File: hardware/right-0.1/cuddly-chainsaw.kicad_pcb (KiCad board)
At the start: 2 copper layers, 3.7 x 3.7 mm, 107 parts, among them J1 USB_C_Receptacle_USB2.0, J2 USB_C_Receptacle_USB2.0, SW1 Encoder_MX_RGB, SW10 MX_RGB, SW11 MX_RGB, SW12 MX_RGB, SW13 MX_RGB, SW14 MX_RGB, SW15 MX_RGB, SW16 MX_RGB, SW17 MX_RGB, SW18 MX_RGB, SW19 MX_RGB, SW2 MX_RGB, SW20 MX_RGB, SW21 MX_RGB, SW22 MX_RGB, SW23 MX_RGB, SW24 MX_RGB, SW25 MX_RGB, SW26 MX_RGB, SW27 MX_RGB, SW28 MX_RGB, SW29 MX_RGB, SW3 MX_RGB, SW30 MX_RGB, SW31 MX_RGB, SW32 MX_RGB, SW33 MX_RGB, SW34 MX_RGB, SW35 SW_Push, SW36 MX_RGB, SW37 MX_RGB, SW38 MX_RGB, SW39 MX_RGB, SW4 MX_RGB, SW40 MX_RGB, SW41 MX_RGB, SW42 MX_RGB, SW5 MX_RGB, SW6 MX_RGB, SW7 MX_RGB, SW8 MX_RGB, SW9 MX_RGB, U1 USBLC6-2SC6, U2 ATmega32U4-MU, Y1 16MHz

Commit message: first go at board outline done
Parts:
- SW14: footprint josh-buttons-switches:MX_KEYSWITCH_RGB -> josh-buttons-switches:MX_KEYSWITCH_RGB_1.75U
- SW37: footprint josh-buttons-switches:MX_KEYSWITCH_RGB -> josh-buttons-switches:MX_KEYSWITCH_RGB_2.5U
- SW6: footprint josh-buttons-switches:MX_KEYSWITCH_RGB -> josh-buttons-switches:MX_KEYSWITCH_RGB_2U
- SW7: footprint josh-buttons-switches:MX_KEYSWITCH_RGB -> josh-buttons-switches:MX_KEYSWITCH_RGB_1.5U
- SW8: footprint josh-buttons-switches:MX_KEYSWITCH_RGB -> josh-buttons-switches:MX_KEYSWITCH_RGB_2.25U
- U2: moved to B.Cu
- moved SW1 184.5 mm to (221.7, 56.3)
- moved SW2 184.5 mm to (221.7, 75.4)
- moved SW4 184.5 mm to (221.7, 113.5)
- moved SW5 184.5 mm to (221.7, 132.5)
- moved SW3 184.5 mm to (221.7, 94.5)
- moved J2 182.1 mm to (78.5, 49.8)
- moved D3 158.3 mm to (202.7, 113.5)
- moved D6 158.2 mm to (221.7, 56.3)
- moved D5 149.1 mm to (193.3, 56.3)
- moved D4 146.7 mm to (191.5, 129.2)
- moved SW10 146.7 mm to (202.7, 132.5)
- moved SW9 146.7 mm to (202.6, 113.5)
- moved SW7 142.0 mm to (197.9, 75.4)
- moved D1 141.9 mm to (186.8, 72.2)
- moved BZ1 139.5 mm to (112.2, 133.2)
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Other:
- board size 3.7 x 3.7 mm -> 181 x 100.8 mm

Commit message: left all connected
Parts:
- added C10: 100n, Capacitor_SMD:C_0603_1608Metric, B.Cu at (265.0, 94.5)
- added C11: 100n, Capacitor_SMD:C_0603_1608Metric, B.Cu at (270.0, 90.5)
- added C12: 100n, Capacitor_SMD:C_0603_1608Metric, B.Cu at (262.5, 98.5)
- added C13: 100n, Capacitor_SMD:C_0603_1608Metric, B.Cu at (256.8, 103.7)
- added C14: 100n, Capacitor_SMD:C_0603_1608Metric, B.Cu at (267.5, 94.5)
- added C15: 100n, Capacitor_SMD:C_0603_1608Metric, B.Cu at (256.8, 123.8)
- added C16: 100n, Capacitor_SMD:C_0603_1608Metric, B.Cu at (256.8, 115.7)
- added C17: 100n, Capacitor_SMD:C_0603_1608Metric, B.Cu at (260.0, 98.5)
- added C18: 100n, Capacitor_SMD:C_0603_1608Metric, B.Cu at (276.6, 90.1)
- added C19: 100n, Capacitor_SMD:C_0603_1608Metric, B.Cu at (256.8, 111.7)
- added C20: 100n, Capacitor_SMD:C_0603_1608Metric, B.Cu at (256.8, 107.7)
- added C21: 100n, Capacitor_SMD:C_0603_1608Metric, B.Cu at (274.1, 90.1)
- added C22: 100n, Capacitor_SMD:C_0603_1608Metric, B.Cu at (270.0, 94.5)
- added C23: 100n, Capacitor_SMD:C_0603_1608Metric, B.Cu at (267.5, 98.5)
- added C24: 100n, Capacitor_SMD:C_0603_1608Metric, B.Cu at (265.0, 98.5)
- added C25: 100n, Capacitor_SMD:C_0603_1608Metric, B.Cu at (260.0, 94.5)
- added C26: 100n, Capacitor_SMD:C_0603_1608Metric, B.Cu at (267.5, 90.5)
- added C27: 100n, Capacitor_SMD:C_0603_1608Metric, B.Cu at (265.0, 90.5)
- added C28: 100n, Capacitor_SMD:C_0603_1608Metric, B.Cu at (262.5, 94.5)
- added C29: 100n, Capacitor_SMD:C_0603_1608Metric, B.Cu at (256.8, 99.7)
- added C8: 100n, Capacitor_SMD:C_0603_1608Metric, B.Cu at (270.0, 98.5)
- added C9: 100n, Capacitor_SMD:C_0603_1608Metric, B.Cu at (256.8, 119.8)
- added D44: WS2812B, LED_SMD:LED_WS2812B_PLCC4_5.0x5.0mm_P3.2mm, B.Cu at (274.6, 121.6)
- added D45: WS2812B, LED_SMD:LED_WS2812B_PLCC4_5.0x5.0mm_P3.2mm, B.Cu at (267.9, 121.6)
- added D46: WS2812B, LED_SMD:LED_WS2812B_PLCC4_5.0x5.0mm_P3.2mm, B.Cu at (274.6, 113.1)
- added D47: WS2812B, LED_SMD:LED_WS2812B_PLCC4_5.0x5.0mm_P3.2mm, B.Cu at (261.3, 121.6)
- added D48: WS2812B, LED_SMD:LED_WS2812B_PLCC4_5.0x5.0mm_P3.2mm, B.Cu at (267.9, 113.1)
- added D49: WS2812B, LED_SMD:LED_WS2812B_PLCC4_5.0x5.0mm_P3.2mm, B.Cu at (274.6, 104.7)
- added D50: WS2812B, LED_SMD:LED_WS2812B_PLCC4_5.0x5.0mm_P3.2mm, B.Cu at (261.3, 113.1)
- added D51: WS2812B, LED_SMD:LED_WS2812B_PLCC4_5.0x5.0mm_P3.2mm, B.Cu at (267.9, 104.7)
- added D52: WS2812B, LED_SMD:LED_WS2812B_PLCC4_5.0x5.0mm_P3.2mm, B.Cu at (274.6, 96.3)
- added D53: WS2812B, LED_SMD:LED_WS2812B_PLCC4_5.0x5.0mm_P3.2mm, B.Cu at (261.3, 104.7)
- added J3: AVR-ISP-6, josh-connectors:AVR_Programmer_SMD, B.Cu at (274.9, 77.6)
- added R9: 22R, Resistor_SMD:R_0603_1608Metric, B.Cu at (250.6, 123.8)
- SW37: footprint josh-buttons-switches:MX_KEYSWITCH_RGB_2.5U -> josh-buttons-switches:MX_KEYSWITCH_RGB_2.5U_REV_STABS
- moved J1 2.52 mm to (154.7, 49.1)
- moved J2 0.80 mm to (78.5, 49.0)
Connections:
- BZ1 pad 1: (no net) -> Net-(BZ1-Pad1)
- U2 pad 10: (no net) -> /32u4 Microcontroller/PB2
- U2 pad 11: (no net) -> /32u4 Microcontroller/PB3
- U2 pad 9: (no net) -> /32u4 Microcontroller/PB1
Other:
- board size 181 x 100.8 mm -> 181.9 x 100.8 mm

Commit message: layout ++
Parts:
- added REF**: MountingHole_3.7mm, MountingHole:MountingHole_3.7mm, F.Cu at (212.1, 123.2)
- added REF**: MountingHole_3.7mm, MountingHole:MountingHole_3.7mm, F.Cu at (174.3, 65.7)
- added REF**: MountingHole_3.7mm, MountingHole:MountingHole_3.7mm, F.Cu at (83.8, 119.2)
- added REF**: MountingHole_3.7mm, MountingHole:MountingHole_3.7mm, F.Cu at (98.0, 65.0)
- moved D52 203.5 mm to (71.2, 104.0), turned to 180 degrees
- moved D51 200.1 mm to (70.4, 136.4), turned to 180 degrees
- moved D53 198.7 mm to (66.5, 65.8), turned to 180 degrees
- moved D50 148.5 mm to (114.6, 136.3), turned to 180 degrees
- moved D49 141.9 mm to (136.2, 136.4), turned to 180 degrees
- moved R4 130.4 mm to (78.0, 57.0), turned to 90 degrees
- moved R3 129.5 mm to (79.5, 57.0), turned to 90 degrees
- moved C15 107.5 mm to (266.5, 16.7)
- moved D48 96.7 mm to (174.1, 136.4), turned to 180 degrees
- moved C9 95.3 mm to (261.5, 24.6)
- moved C16 95.3 mm to (261.5, 20.5)
- moved BZ1 89.9 mm to (186.8, 83.0), turned to 180 degrees
- moved C13 87.3 mm to (264.0, 16.7)
- moved C19 84.7 mm to (271.5, 28.3)
- moved C29 83.0 mm to (261.5, 16.8)
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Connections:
- D11 pad 1: (no net) -> +5V
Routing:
- net /ROW_5: track 0.00 -> 137.5 mm
- net /ROW_2: track 0.00 -> 131.6 mm
- net /ROW_4: track 0.00 -> 122.3 mm
- net /ROW_3: track 0.00 -> 110.2 mm
- net /ROW_1: track 0.00 -> 67.9 mm
- net Net-(D2-Pad2): track 0.00 -> 55.5 mm
- net Net-(D5-Pad2): track 0.00 -> 52.1 mm
- net GND: track 0.00 -> 44.3 mm, vias 0 -> 23
- net Net-(D1-Pad2): track 0.00 -> 41.6 mm, vias 0 -> 2
- net Net-(D3-Pad2): track 0.00 -> 33.9 mm
- net Net-(D4-Pad2): track 0.00 -> 30.6 mm
- net VBUS: track 0.00 -> 30.3 mm, vias 0 -> 2
- net Net-(F1-Pad2): track 0.00 -> 29.9 mm
- net Net-(D35-Pad2): track 0.00 -> 29.0 mm
- net +5V: track 0.00 -> 26.1 mm
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- added copper zone on B.Cu, net +5V
- added copper zone on F.Cu, net GND

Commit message: right half passes drc
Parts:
- moved C26 225.2 mm to (55.3, 80.2), turned to 270 degrees
- moved C10 208.0 mm to (64.8, 61.1), turned to 270 degrees
- moved C9 205.6 mm to (88.5, 135.7)
- moved C21 203.6 mm to (77.0, 103.2), turned to 270 degrees
- moved C11 191.9 mm to (92.5, 79.4), turned to 180 degrees
- moved C20 189.0 mm to (98.1, 97.6)
- moved C17 180.2 mm to (121.9, 135.7)
- moved C8 173.2 mm to (140.9, 135.7)
- moved C15 173.1 mm to (126.0, 117.8), turned to 180 degrees
- moved C16 163.3 mm to (102.9, 59.5)
- moved C22 155.1 mm to (130.4, 79.4), turned to 180 degrees
- moved C19 153.2 mm to (135.3, 98.4), turned to 180 degrees
- moved C12 139.4 mm to (180.4, 134.4)
- moved C23 133.0 mm to (198.1, 135.7)
- moved C28 132.1 mm to (140.3, 60.3), turned to 180 degrees
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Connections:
- D44 pad 4: (no net) -> /LED_UNDER
- R9 pad 2: (no net) -> /PIEZO
- SW1 pad 1: (no net) -> /LED_KEYS
- SW1 pad A: (no net) -> /ENC_A
- SW1 pad B: (no net) -> /ENC_B
- SW42 pad 2: (no net) -> /COL_9
- U2 pad 1: (no net) -> /LED_KEYS
- U2 pad 12: (no net) -> /PIEZO
- U2 pad 20: (no net) -> /COL_1
- U2 pad 21: (no net) -> /COL_2
- U2 pad 22: (no net) -> /COL_3
- U2 pad 25: (no net) -> /COL_4
- U2 pad 26: (no net) -> /COL_5
- U2 pad 27: (no net) -> /COL_6
- U2 pad 28: (no net) -> /COL_7
- U2 pad 29: (no net) -> /COL_8
- U2 pad 31: (no net) -> /ROW_5
- U2 pad 32: (no net) -> /ROW_4
- U2 pad 36: (no net) -> /ROW_3
- U2 pad 37: (no net) -> /ROW_2
- U2 pad 38: (no net) -> /ROW_1
- U2 pad 39: (no net) -> /ENC_A
- U2 pad 40: (no net) -> /ENC_B
- U2 pad 41: (no net) -> /LED_UNDER
- U2 pad 8: (no net) -> /COL_9
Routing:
- net /COL_8: track 0.00 -> 318.4 mm, vias 0 -> 3
- net /COL_7: track 0.00 -> 268.5 mm, vias 0 -> 2
- net /COL_6: track 0.00 -> 242.4 mm, vias 0 -> 2
- net /COL_5: track 0.00 -> 223.7 mm, vias 0 -> 2
- net /COL_4: track 0.00 -> 198.7 mm, vias 0 -> 2
- net /COL_9: track 0.00 -> 193.4 mm, vias 0 -> 2
- net /DAT_2: track 0.00 -> 184.3 mm, vias 0 -> 2
- net /DAT_3: track 0.00 -> 184.2 mm, vias 0 -> 2
- net /DAT_4: track 0.00 -> 180.2 mm
- net /DAT_1: track 0.00 -> 179.9 mm, vias 0 -> 4
- net /COL_3: track 0.00 -> 173.6 mm, vias 0 -> 2
- net /SDA: track 7.48 -> 174.2 mm, vias 0 -> 4
- net /SCL_SERIAL: track 6.47 -> 173.1 mm, vias 0 -> 4
- net /COL_2: track 0.00 -> 133.4 mm, vias 0 -> 2
- net /COL_1: track 2.04 -> 104.8 mm
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
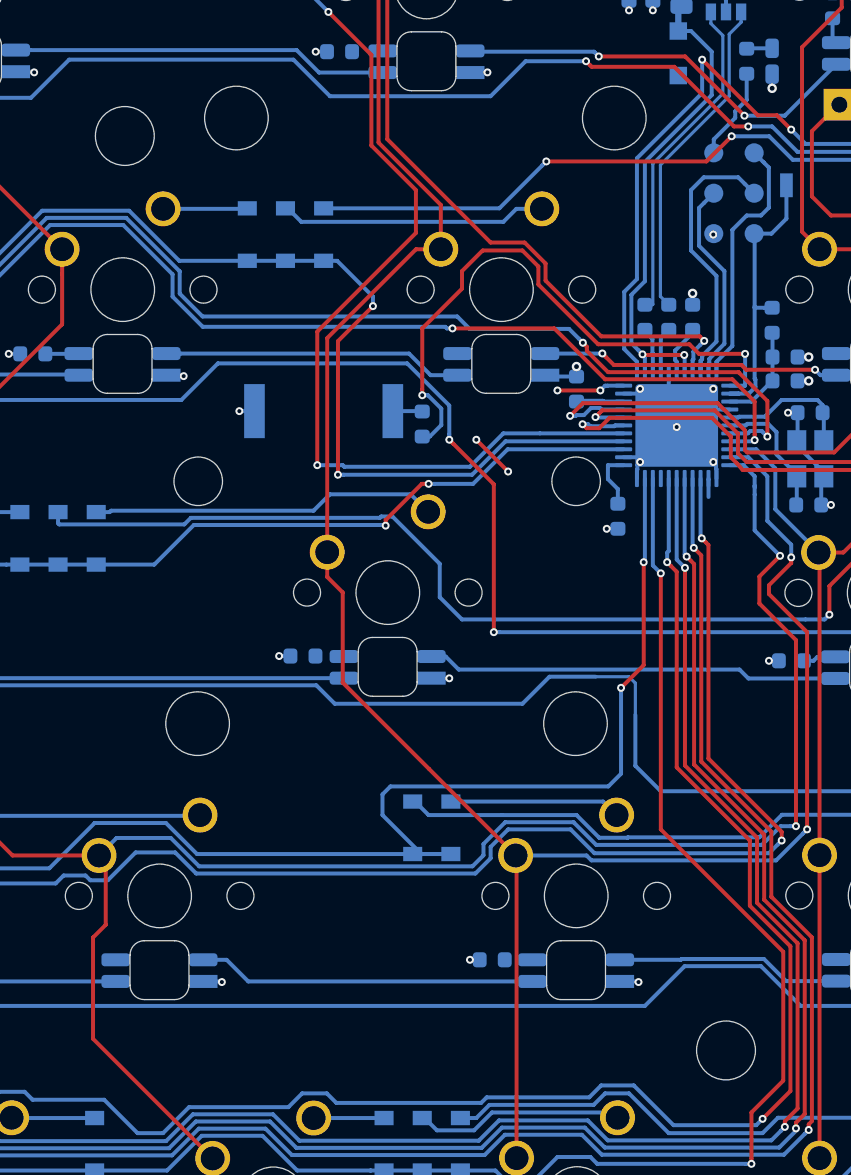
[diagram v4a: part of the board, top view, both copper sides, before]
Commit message: moved mounting oles
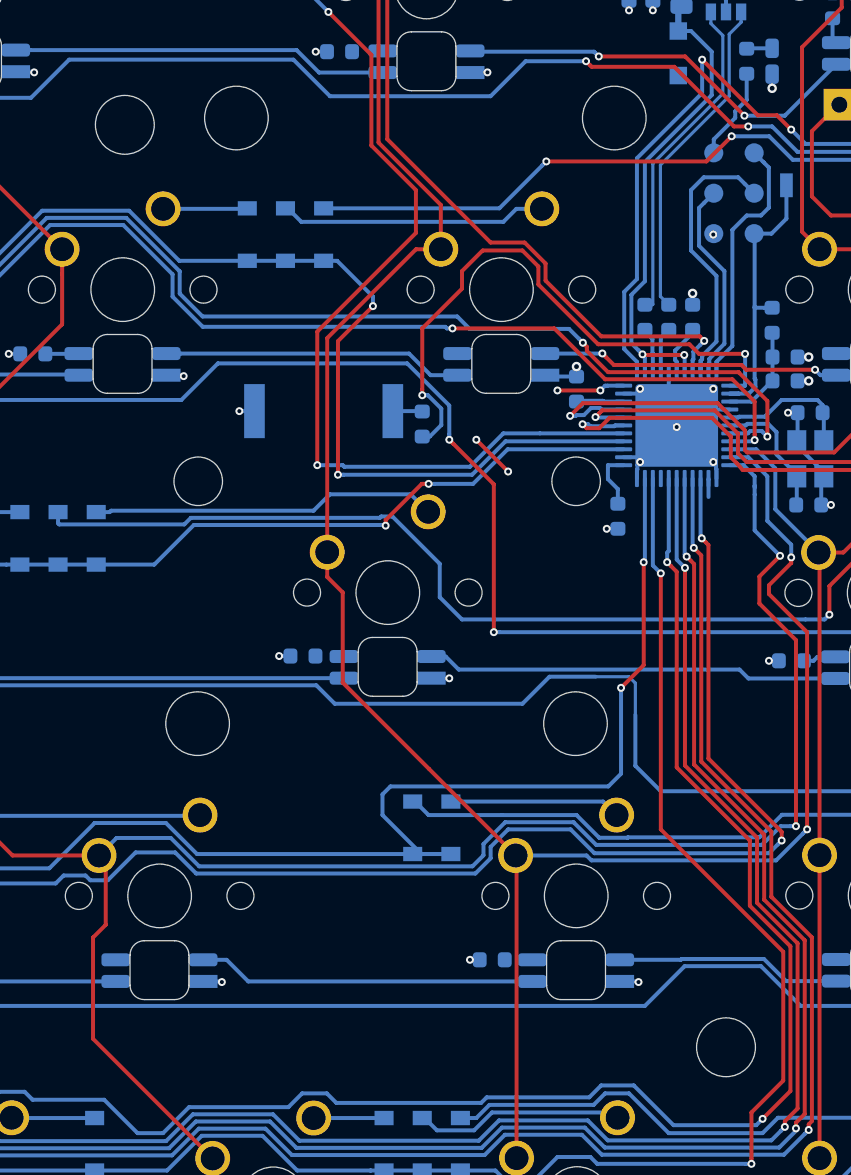
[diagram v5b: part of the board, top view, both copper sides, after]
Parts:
- moved REF** 0.70 mm to (174.3, 65.0)
- moved REF** 0.20 mm to (212.1, 123.0)
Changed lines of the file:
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@@
   )
   (setup
-    (last_trace_width 0.2)
+    (last_trace_width 0.25)
     (user_trace_width 0.2)
     (user_trace_width 0.3)
@@
   )
   (module MountingHole:MountingHole_3.7mm (layer F.Cu)
-    (at 212.1 123.2)
+    (at 212.1 123)
     (descr "Mounting Hole 3.7mm, no annular")
     (tags "mounting hole 3.7mm no annular")
@@
   )
   (module MountingHole:MountingHole_3.7mm (layer F.Cu)
-    (at 174.3 65.7)
+    (at 174.3 65)
     (descr "Mounting Hole 3.7mm, no annular")
     (tags "mounting hole 3.7mm no annular")
@@
   (gr_arc (start 51.5 143) (end 49.5 143) (angle -90) (layer Edge.Cuts) (width 0.05))
   (gr_line (start 51.5 145) (end 229.4 144.9) (layer Edge.Cuts) (width 0.05))
-  (segment (start 212.3375 86.4) (end 213.2 86.4) (width 0.25) (layer B.Cu) (net 77))
-  (segment (start 213.2 86.4) (end 213.9 87.1) (width 0.25) (layer B.Cu) (net 77))
   (via (at 209 84) (size 0.5) (drill 0.25) (layers F.Cu B.Cu) (net 1))
   (via (at 206.7 86.2) (size 0.5) (drill 0.25) (layers F.Cu B.Cu) (net 1))
@@
   (segment (start 155.1 60.3) (end 148.39125 60.3) (width 0.25) (layer B.Cu) (net 76))
   (segment (start 156.46 61.66) (end 155.1 60.3) (width 0.25) (layer B.Cu) (net 76))
+  (segment (start 212.3375 86.4) (end 213.2 86.4) (width 0.25) (layer B.Cu) (net 77))
+  (segment (start 213.2 86.4) (end 213.9 87.1) (width 0.25) (layer B.Cu) (net 77))
   (segment (start 173.1 111.36375) (end 172.6775 110.94125) (width 0.25) (layer F.Cu) (net 77))
   (segment (start 173.1 115.3) (end 173.1 111.36375) (width 0.25) (layer F.Cu) (net 77))

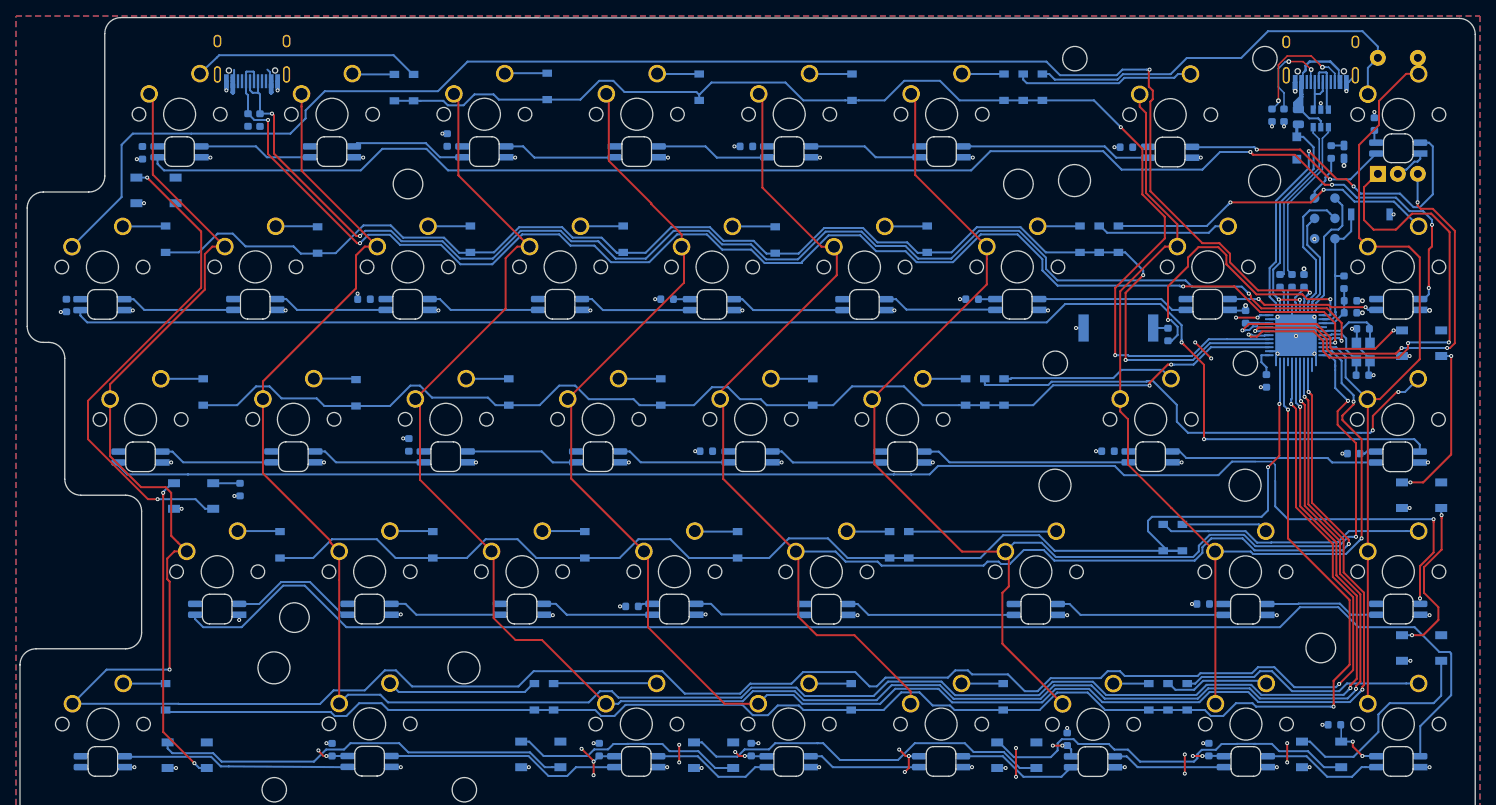
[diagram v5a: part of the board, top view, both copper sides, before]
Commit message: updated components due to jlk change
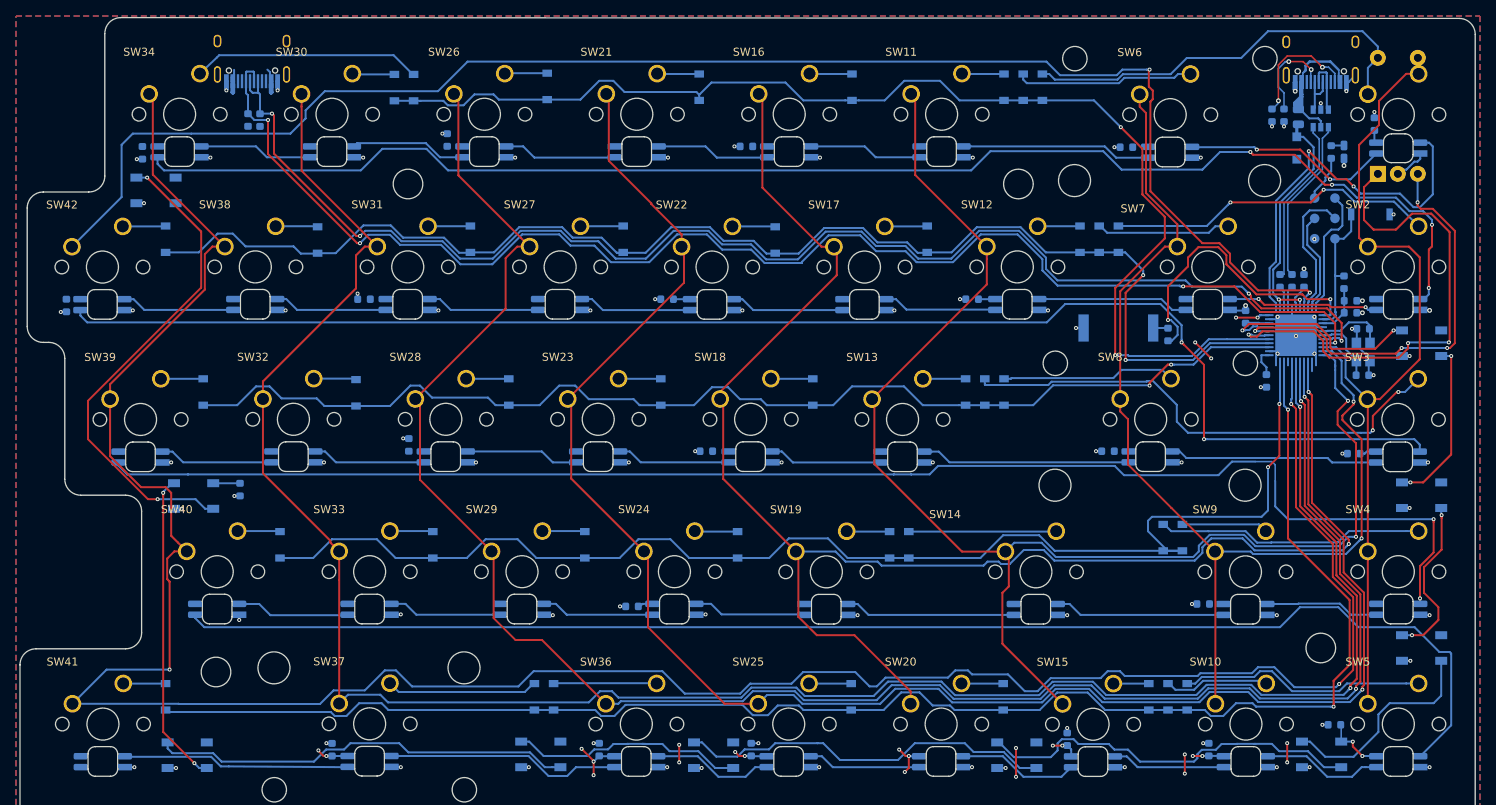
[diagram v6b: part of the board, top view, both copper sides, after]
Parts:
- J3: footprint josh-connectors:AVR_Programmer_SMD -> josh-connectors:AVR_PROG_2.54_SMT
- SW10, SW11, SW12, SW13, SW15, SW16, SW17, SW18, SW19, SW2, SW20, SW21, SW22, SW23, SW24, SW25, SW26, SW27, SW28, SW29, SW3, SW30, SW31, SW32, SW33, SW34, SW36, SW38, SW39, SW4, SW40, SW41, SW42, SW5, SW9: footprint josh-buttons-switches:MX_KEYSWITCH_RGB -> josh-keyboard:MX_KEYSWITCH_RGB
- SW14: footprint josh-buttons-switches:MX_KEYSWITCH_RGB_1.75U -> josh-keyboard:MX_KEYSWITCH_RGB_1.75U
- SW35: footprint josh-buttons-switches:BT_Small_2_Pin -> josh-buttons-switches:SW_Push_PTS820
- SW37: footprint josh-buttons-switches:MX_KEYSWITCH_RGB_2.5U_REV_STABS -> josh-keyboard:MX_KEYSWITCH_RGB_2.5U_REV_STABS
- SW6: footprint josh-buttons-switches:MX_KEYSWITCH_RGB_2U -> josh-keyboard:MX_KEYSWITCH_RGB_2U
- SW7: footprint josh-buttons-switches:MX_KEYSWITCH_RGB_1.5U -> josh-keyboard:MX_KEYSWITCH_RGB_1.5U
- SW8: footprint josh-buttons-switches:MX_KEYSWITCH_RGB_2.25U -> josh-keyboard:MX_KEYSWITCH_RGB_2.25U
- moved REF** 11.9 mm to (74.0, 126.0)
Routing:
- net /DAT_4: track 180.2 -> 175.8 mm
- net Net-(SW33-Pad4): track 16.6 -> 14.3 mm
